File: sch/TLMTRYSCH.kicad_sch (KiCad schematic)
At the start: 7 parts, among them J11 Antenna, U11 SI2301DS, U12 RFM95W-868S2, U13 uBlox_NEO-6M_Breakout

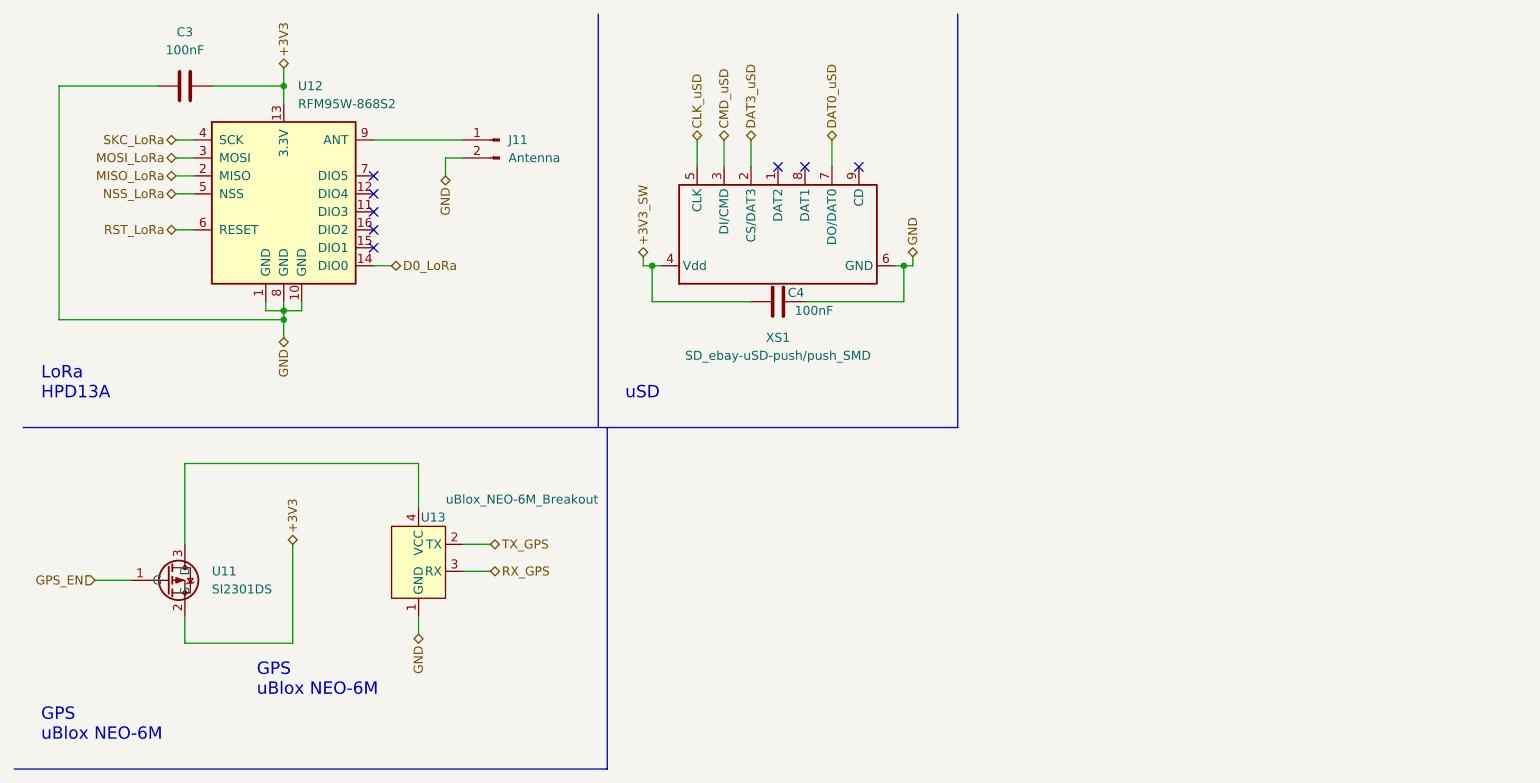
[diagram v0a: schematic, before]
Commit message: Diseño actualizado - MK4
Diseño actualizado para cumplir con la nueva misión. Se elimino una placa, el sensor de calidad de aire, servos y sensor de humedad
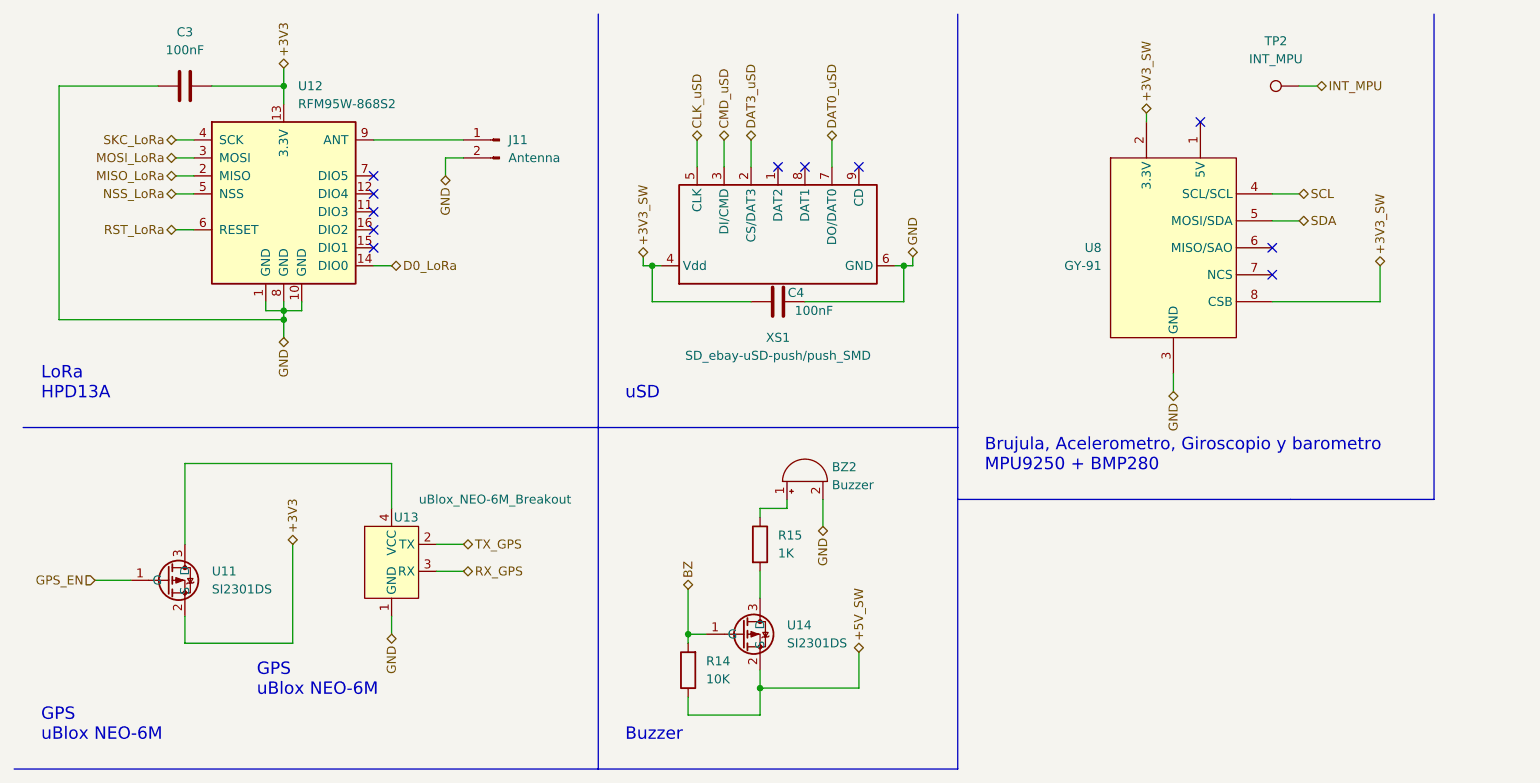
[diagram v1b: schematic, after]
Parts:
- added BZ2: Buzzer, Buzzer_Beeper:Buzzer_12x9.5RM7.6, symbol Device:Buzzer
- added R14: 10K, Resistor_SMD:R_0805_2012Metric_Pad1.20x1.40mm_HandSolder, symbol Device:R
- added R15: 1K, Resistor_SMD:R_0805_2012Metric_Pad1.20x1.40mm_HandSolder, symbol Device:R
- added TP2: INT_MPU, TestPoint:TestPoint_THTPad_D1.5mm_Drill0.7mm, symbol Connector:TestPoint
- added U14: SI2301DS, Package_TO_SOT_SMD:SOT-23, symbol mCALCAN_lib:SI2301DS
- added U8: GY-91, mCALCAN_lib:GY-91_Breakout, symbol mCALCAN_lib:GY-91
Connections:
- net +3V3_SW: now also U8.2 (3.3V), U8.8 (CSB)
- net GND: now also BZ2.2 (+), U8.3 (GND)
- new net: BZ2.1 (-), R15.1
- new net: R15.2, U14.3 (D)
- new net +5V_SW: R14.1, U14.2 (S)
- new net BZ: R14.2, U14.1 (G)
- new net INT_MPU: TP2.1
- new net SCL: U8.4 (SCL/SCL)
- new net SDA: U8.5 (MOSI/SDA)
- no-connect marks 8 -> 11
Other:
- note added: "Brujula, Acelerometro, Giroscopio y barometro MPU9250 + BMP280"
- note added: "Buzzer"
- moved on the sheet: U13
